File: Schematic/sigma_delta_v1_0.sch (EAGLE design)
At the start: 64 parts, among them IC1 LM50, IC2 MC78M12CDTG, IC3 UA78M33DCY, IC4 LM50, IC5 ACPL-064L-000E, J1 SJ1-3523N, Q3 IRF3707S, Q4 IRF3707S, Q5 BSD223P, X1 1751251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

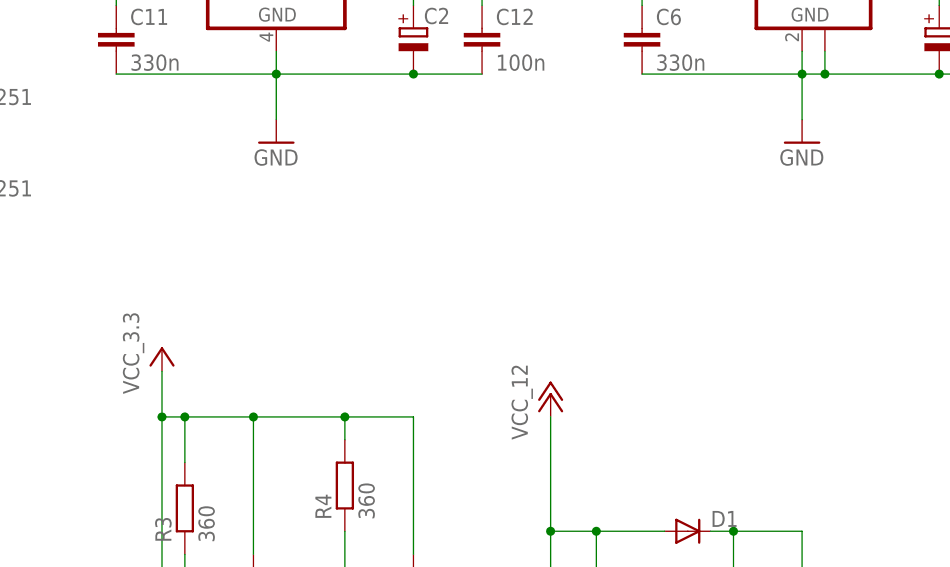
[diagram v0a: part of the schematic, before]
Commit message: added comment to the scematic regarding the inverter stage
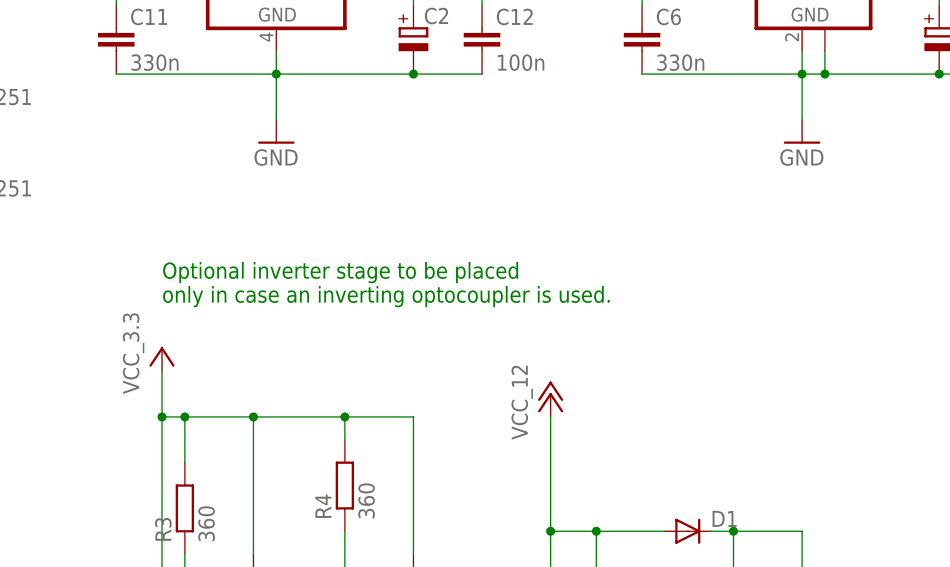
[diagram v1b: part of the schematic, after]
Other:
- note added: "Optional inverter stage to be placed only in case an inverting optocoupler is used."
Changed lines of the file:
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@@
 <grid distance="0.1" unitdist="inch" unit="inch" style="lines" multiple="1" display="no" altdistance="0.01" altunitdist="inch" altunit="inch"/>
 <layers>
-<layer number="1" name="Top" color="4" fill="1" visible="no" active="no"/>
-<layer number="2" name="Route2" color="1" fill="3" visible="no" active="no"/>
-<layer number="3" name="Route3" color="4" fill="3" visible="no" active="no"/>
-<layer number="4" name="Route4" color="1" fill="4" visible="no" active="no"/>
-<layer number="5" name="Route5" color="4" fill="4" visible="no" active="no"/>
-<layer number="6" name="Route6" color="1" fill="8" visible="no" active="no"/>
-<layer number="7" name="Route7" color="4" fill="8" visible="no" active="no"/>
-<layer number="8" name="Route8" color="1" fill="2" visible="no" active="no"/>
-<layer number="9" name="Route9" color="4" fill="2" visible="no" active="no"/>
-<layer number="10" name="Route10" color="1" fill="7" visible="no" active="no"/>
-<layer number="11" name="Route11" color="4" fill="7" visible="no" active="no"/>
-<layer number="12" name="Route12" color="1" fill="5" visible="no" active="no"/>
-<layer number="13" name="Route13" color="4" fill="5" visible="no" active="no"/>
-<layer number="14" name="Route14" color="1" fill="6" visible="no" active="no"/>
-<layer number="15" name="Route15" color="4" fill="6" visible="no" active="no"/>
-<layer number="16" name="Bottom" color="1" fill="1" visible="no" active="no"/>
-<layer number="17" name="Pads" color="2" fill="1" visible="no" active="no"/>
-<layer number="18" name="Vias" color="2" fill="1" visible="no" active="no"/>
-<layer number="19" name="Unrouted" color="6" fill="1" visible="no" active="no"/>
-<layer number="20" name="Dimension" color="15" fill="1" visible="no" active="no"/>
-<layer number="21" name="tPlace" color="7" fill="1" visible="no" active="no"/>
-<layer number="22" name="bPlace" color="7" fill="1" visible="no" active="no"/>
-<layer number="23" name="tOrigins" color="15" fill="1" visible="no" active="no"/>
-<layer number="24" name="bOrigins" color="15" fill="1" visible="no" active="no"/>
-<layer number="25" name="tNames" color="7" fill="1" visible="no" active="no"/>
-<layer number="26" name="bNames" color="7" fill="1" visible="no" active="no"/>
-<layer number="27" name="tValues" color="7" fill="1" visible="no" active="no"/>
-<layer number="28" name="bValues" color="7" fill="1" visible="no" active="no"/>
+<layer number="1" name="Top" color="4" fill="1" visible="yes" active="no"/>
+<layer number="2" name="Route2" color="1" fill="3" visible="yes" active="no"/>
+<layer number="3" name="Route3" color="4" fill="3" visible="yes" active="no"/>
+<layer number="4" name="Route4" color="1" fill="4" visible="yes" active="no"/>
+<layer number="5" name="Route5" color="4" fill="4" visible="yes" active="no"/>
+<layer number="6" name="Route6" color="1" fill="8" visible="yes" active="no"/>
+<layer number="7" name="Route7" color="4" fill="8" visible="yes" active="no"/>
+<layer number="8" name="Route8" color="1" fill="2" visible="yes" active="no"/>
+<layer number="9" name="Route9" color="4" fill="2" visible="yes" active="no"/>
+<layer number="10" name="Route10" color="1" fill="7" visible="yes" active="no"/>
+<layer number="11" name="Route11" color="4" fill="7" visible="yes" active="no"/>
+<layer number="12" name="Route12" color="1" fill="5" visible="yes" active="no"/>
+<layer number="13" name="Route13" color="4" fill="5" visible="yes" active="no"/>
+<layer number="14" name="Route14" color="1" fill="6" visible="yes" active="no"/>
+<layer number="15" name="Route15" color="4" fill="6" visible="yes" active="no"/>
+<layer number="16" name="Bottom" color="1" fill="1" visible="yes" active="no"/>
+<layer number="17" name="Pads" color="2" fill="1" visible="yes" active="no"/>
+<layer number="18" name="Vias" color="2" fill="1" visible="yes" active="no"/>
+<layer number="19" name="Unrouted" color="6" fill="1" visible="yes" active="no"/>
+<layer number="20" name="Dimension" color="15" fill="1" visible="yes" active="no"/>
+<layer number="21" name="tPlace" color="7" fill="1" visible="yes" active="no"/>
+<layer number="22" name="bPlace" color="7" fill="1" visible="yes" active="no"/>
+<layer number="23" name="tOrigins" color="15" fill="1" visible="yes" active="no"/>
+<layer number="24" name="bOrigins" color="15" fill="1" visible="yes" active="no"/>
+<layer number="25" name="tNames" color="7" fill="1" visible="yes" active="no"/>
+<layer number="26" name="bNames" color="7" fill="1" visible="yes" active="no"/>
+<layer number="27" name="tValues" color="7" fill="1" visible="yes" active="no"/>
+<layer number="28" name="bValues" color="7" fill="1" visible="yes" active="no"/>
 <layer number="29" name="tStop" color="7" fill="3" visible="no" active="no"/>
 <layer number="30" name="bStop" color="7" fill="6" visible="no" active="no"/>
@@
 <layer number="35" name="tGlue" color="7" fill="4" visible="no" active="no"/>
 <layer number="36" name="bGlue" color="7" fill="5" visible="no" active="no"/>
-<layer number="37" name="tTest" color="7" fill="1" visible="no" active="no"/>
-<layer number="38" name="bTest" color="7" fill="1" visible="no" active="no"/>
+<layer number="37" name="tTest" color="7" fill="1" visible="yes" active="no"/>
+<layer number="38" name="bTest" color="7" fill="1" visible="yes" active="no"/>
 <layer number="39" name="tKeepout" color="4" fill="11" visible="no" active="no"/>
 <layer number="40" name="bKeepout" color="1" fill="11" visible="no" active="no"/>
@@
 <layer number="44" name="Drills" color="7" fill="1" visible="no" active="no"/>
 <layer number="45" name="Holes" color="7" fill="1" visible="no" active="no"/>
-<layer number="46" name="Milling" color="3" fill="1" visible="no" active="no"/>
-<layer number="47" name="Measures" color="7" fill="1" visible="no" active="no"/>
-<layer number="48" name="Document" color="7" fill="1" visible="no" active="no"/>
-<layer number="49" name="Reference" color="7" fill="1" visible="no" active="no"/>
-<layer number="51" name="tDocu" color="7" fill="1" visible="no" active="no"/>
-<layer number="52" name="bDocu" color="7" fill="1" visible="no" active="no"/>
+<layer number="46" name="Milling" color="3" fill="1" visible="yes" active="no"/>
+<layer number="47" name="Measures" color="7" fill="1" visible="yes" active="no"/>
+<layer number="48" name="Document" color="7" fill="1" visible="yes" active="no"/>
+<layer number="49" name="Reference" color="7" fill="1" visible="yes" active="no"/>
+<layer number="51" name="tDocu" color="7" fill="1" visible="yes" active="no"/>
+<layer number="52" name="bDocu" color="7" fill="1" visible="yes" active="no"/>
 <layer number="90" name="Modules" color="5" fill="1" visible="yes" active="yes"/>
 <layer number="91" name="Nets" color="2" fill="1" visible="yes" active="yes"/>
@@
 transistors</text>
 <text x="93.98" y="241.3" size="1.778" layer="91">See maximum current estimation</text>
+<text x="154.94" y="200.66" size="1.778" layer="91">Optional inverter stage to be placed
+only in case an inverting optocoupler is used.</text>
 </plain>
 <instances>
